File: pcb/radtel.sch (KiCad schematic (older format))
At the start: 51 parts, among them IC1 ADP3335, IC2 Si4460, IC3 STM32F072CBT6, P1 PWR, P2 UART, P3 USB_OTG, P4 SWD, P5 ANTENNA, Y1 26MHz, Y2 8MHz

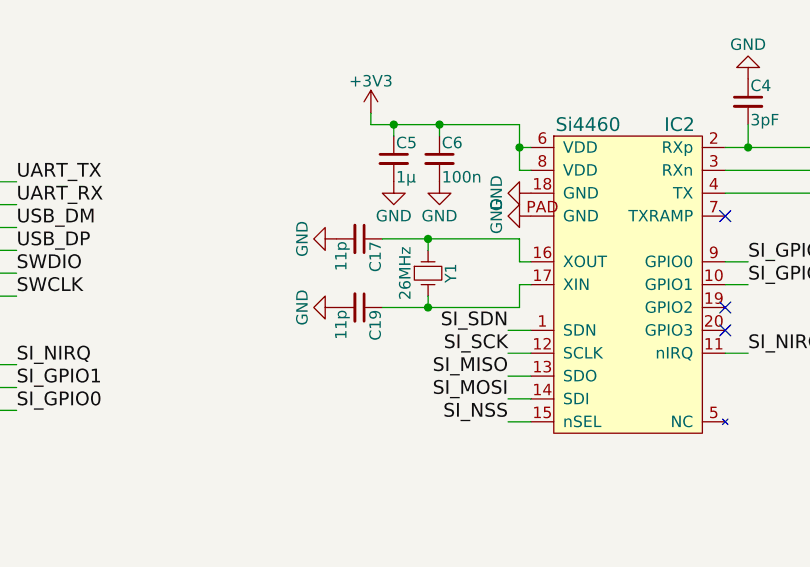
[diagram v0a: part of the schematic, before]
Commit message: remove caps on radio xtal as not needed
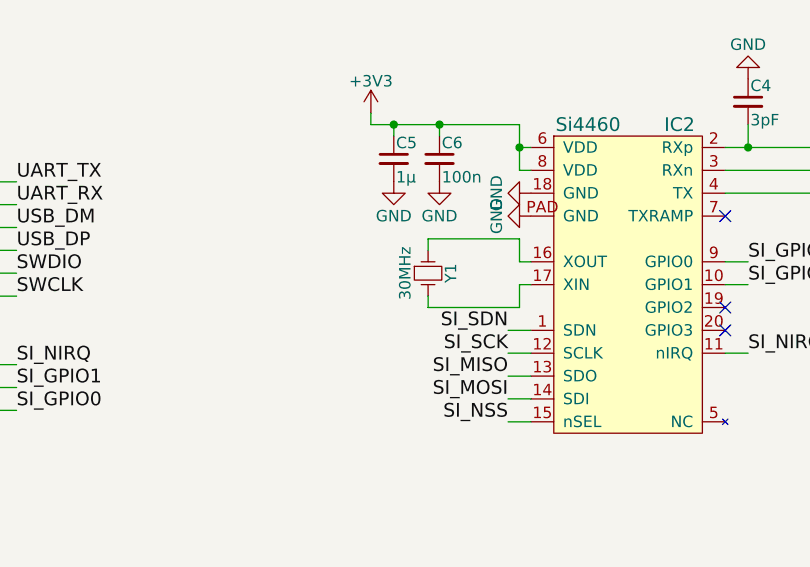
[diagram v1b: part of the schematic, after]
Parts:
- removed C17, C19: 11p, radtel:C0603, symbol C_Small
- Y1: value 26MHz -> 30MHz
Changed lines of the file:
@@
 LIBS:swd
 LIBS:si4460
+LIBS:radtel-cache
 EELAYER 25 0
 EELAYER END
@@
 P 5450 3550
 F 0 "Y1" H 5450 3650 50  0000 C CNN
-F 1 "26MHz" H 5450 3450 50  0000 C CNN
+F 1 "30MHz" H 5450 3450 50  0000 C CNN
 F 2 "radtel:XTAL50x32" H 5450 3550 60  0001 C CNN
 F 3 "" H 5450 3550 60  0000 C CNN
@@
 NoConn ~ 3550 5350
 $Comp
-L C_Small C17
-U 1 1 563F3EBE
-P 5150 3400
-F 0 "C17" H 5160 3470 50  0000 L CNN
-F 1 "11p" H 5160 3320 50  0000 L CNN
-F 2 "radtel:C0603" H 5150 3400 60  0001 C CNN
-F 3 "" H 5150 3400 60  0000 C CNN
-	1    5150 3400
-	0    1    1    0
-$EndComp
-$Comp
-L C_Small C19
-U 1 1 563F3F5F
-P 5150 3700
-F 0 "C19" H 5160 3770 50  0000 L CNN
-F 1 "11p" H 5160 3620 50  0000 L CNN
-F 2 "radtel:C0603" H 5150 3700 60  0001 C CNN
-F 3 "" H 5150 3700 60  0000 C CNN
-	1    5150 3700
-	0    1    1    0
-$EndComp
-$Comp
 L C_Small C6
 U 1 1 563F412D
@@
 	1    5300 3050
 	1    0    0    -1
-$EndComp
-$Comp
-L GND #PWR027
-U 1 1 563F4C5C
-P 5050 3700
-F 0 "#PWR027" H 5050 3450 50  0001 C CNN
-F 1 "GND" H 5050 3550 50  0000 C CNN
-F 2 "" H 5050 3700 60  0000 C CNN
-F 3 "" H 5050 3700 60  0000 C CNN
-	1    5050 3700
-	0    1    1    0
-$EndComp
-$Comp
-L GND #PWR028
-U 1 1 563F4D57
-P 5050 3400
-F 0 "#PWR028" H 5050 3150 50  0001 C CNN
-F 1 "GND" H 5050 3250 50  0000 C CNN
-F 2 "" H 5050 3400 60  0000 C CNN
-F 3 "" H 5050 3400 60  0000 C CNN
-	1    5050 3400
-	0    1    1    0
 $EndComp
 $Comp
@@
 	5850 3600 5850 3700
 Wire Wire Line
-	5850 3700 5250 3700
-Wire Wire Line
-	5250 3400 5850 3400
-Wire Wire Line
 	5850 3400 5850 3500
 Wire Wire Line
@@
 Wire Wire Line
 	5450 3450 5450 3400
-Connection ~ 5450 3400
 Wire Wire Line
 	5450 3650 5450 3700
-Connection ~ 5450 3700
 Wire Wire Line
 	5200 2850 5200 2900
@@
 Wire Wire Line
 	3650 3950 3550 3950
+Wire Wire Line
+	5450 3400 5850 3400
+Wire Wire Line
+	5450 3700 5850 3700
 $EndSCHEMATC

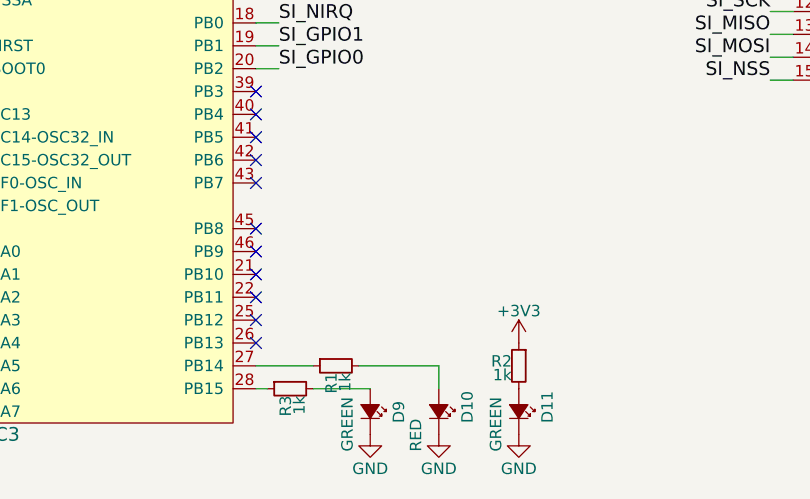
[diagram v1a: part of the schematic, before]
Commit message: add farnell numbers
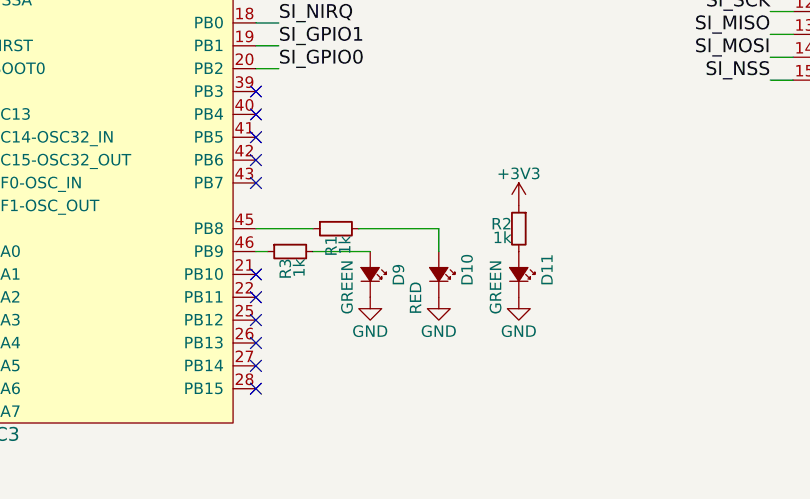
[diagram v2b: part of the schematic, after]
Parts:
- C1, C10, C2, C5: Farnell (none) -> 2346895
- C11, C12, C20, C6: Farnell (none) -> 1759122
- C13: Farnell (none) -> 2112704
- C21, C22: Farnell (none) -> 1759055
- C3: Farnell (none) -> 1414605
- C8, C9: Farnell (none) -> 2211164
- D1, D2, D3, D4, D5, D6, D7, D8: Farnell (none) -> 2368173
- D10: Farnell (none) -> 2290329
- D11, D9: Farnell (none) -> 2290328
- IC1: Farnell (none) -> 2067775
- IC2: Farnell (none) -> 2462635
- IC3: Farnell (none) -> 2432094
- P1: Farnell (none) -> 1830747
- P2: Farnell (none) -> 1830749
- P3: Farnell (none) -> 2443111
- P4: Farnell (none) -> 1667759
- R1, R2, R3: Farnell (none) -> 2116678
- Y1: Farnell (none) -> 1611809
- Y2: Farnell (none) -> 2101329
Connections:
- net at IC3.27 (PB14): no longer R1.1
- net at IC3.28 (PB15): no longer R3.1
- net at IC3.45 (PB8): now also R1.1
- net at IC3.46 (PB9): now also R3.1
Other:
- moved on the sheet: D10, D11, D9, R1, R2, R3
